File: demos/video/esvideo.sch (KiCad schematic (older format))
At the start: 29 parts, among them U8 BT253, U9 BT473

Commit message: Pcbnew: Minor fix in hotkeys. Demos: add an example to use  a local fp-lib-table and local libs, and update schematics and boards.
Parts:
- C32, C33, C34, C35, C36, C37, C52, R15, R22, R23, R24, R36, R37, R38, R42, R43, R44, R45, R46, R47, R8: footprint (none) -> lib_smd:SM1206
- C39, C40, C41, C42, C51: footprint (none) -> lib_smd:SM1210L
- L5: footprint (none) -> lib_smd:SM1812
- U8: footprint (none) -> footprints:PLCC84
- U9: footprint (none) -> footprints:PLCC68

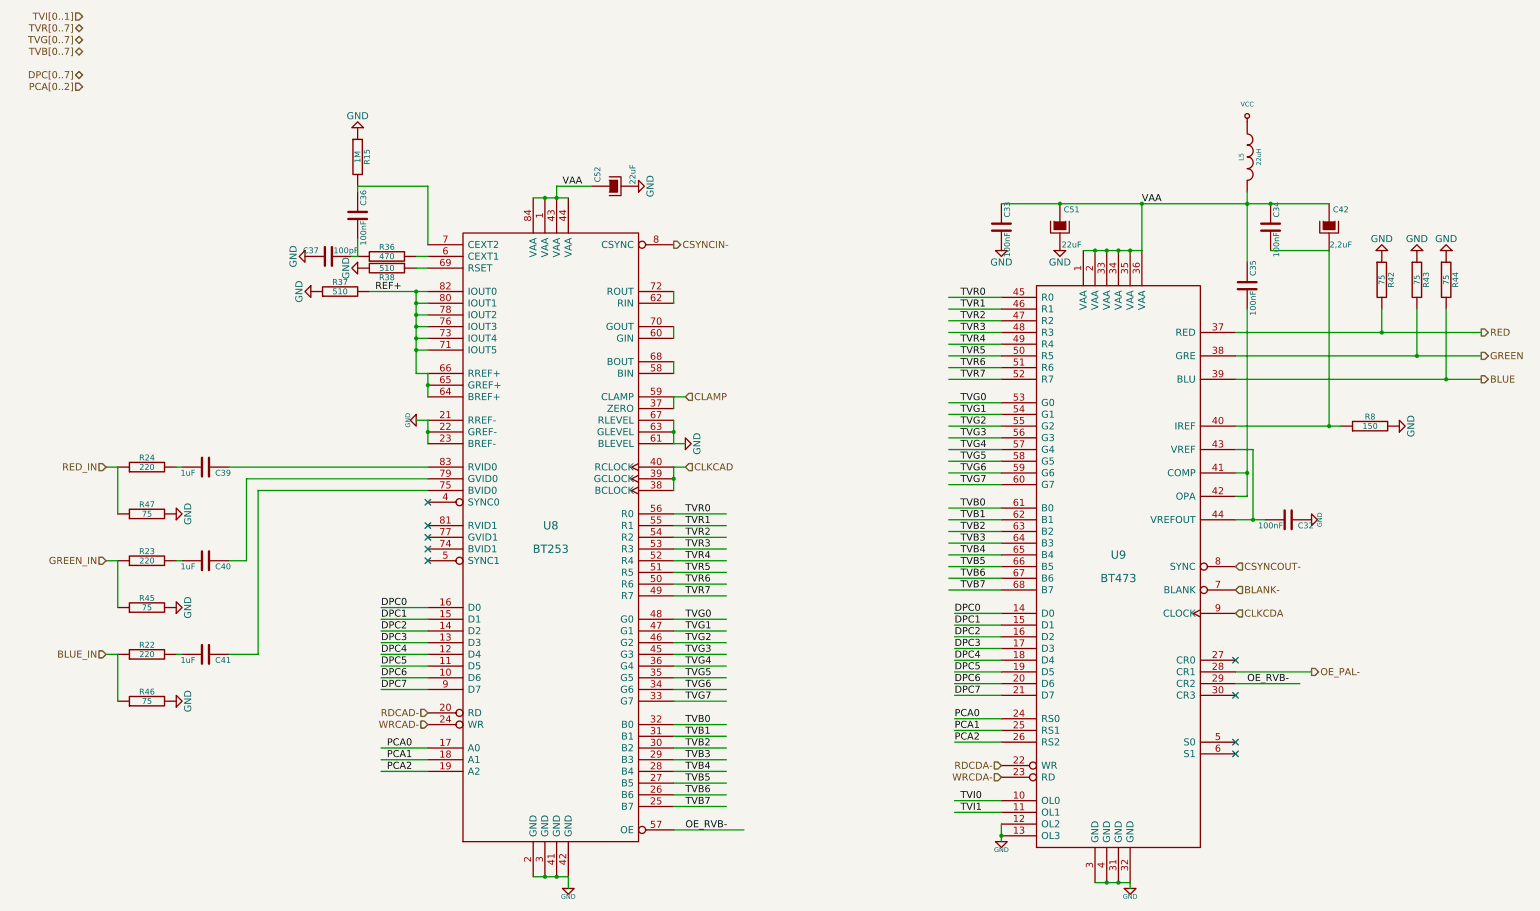
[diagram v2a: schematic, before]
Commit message: demos/ schematic tidying
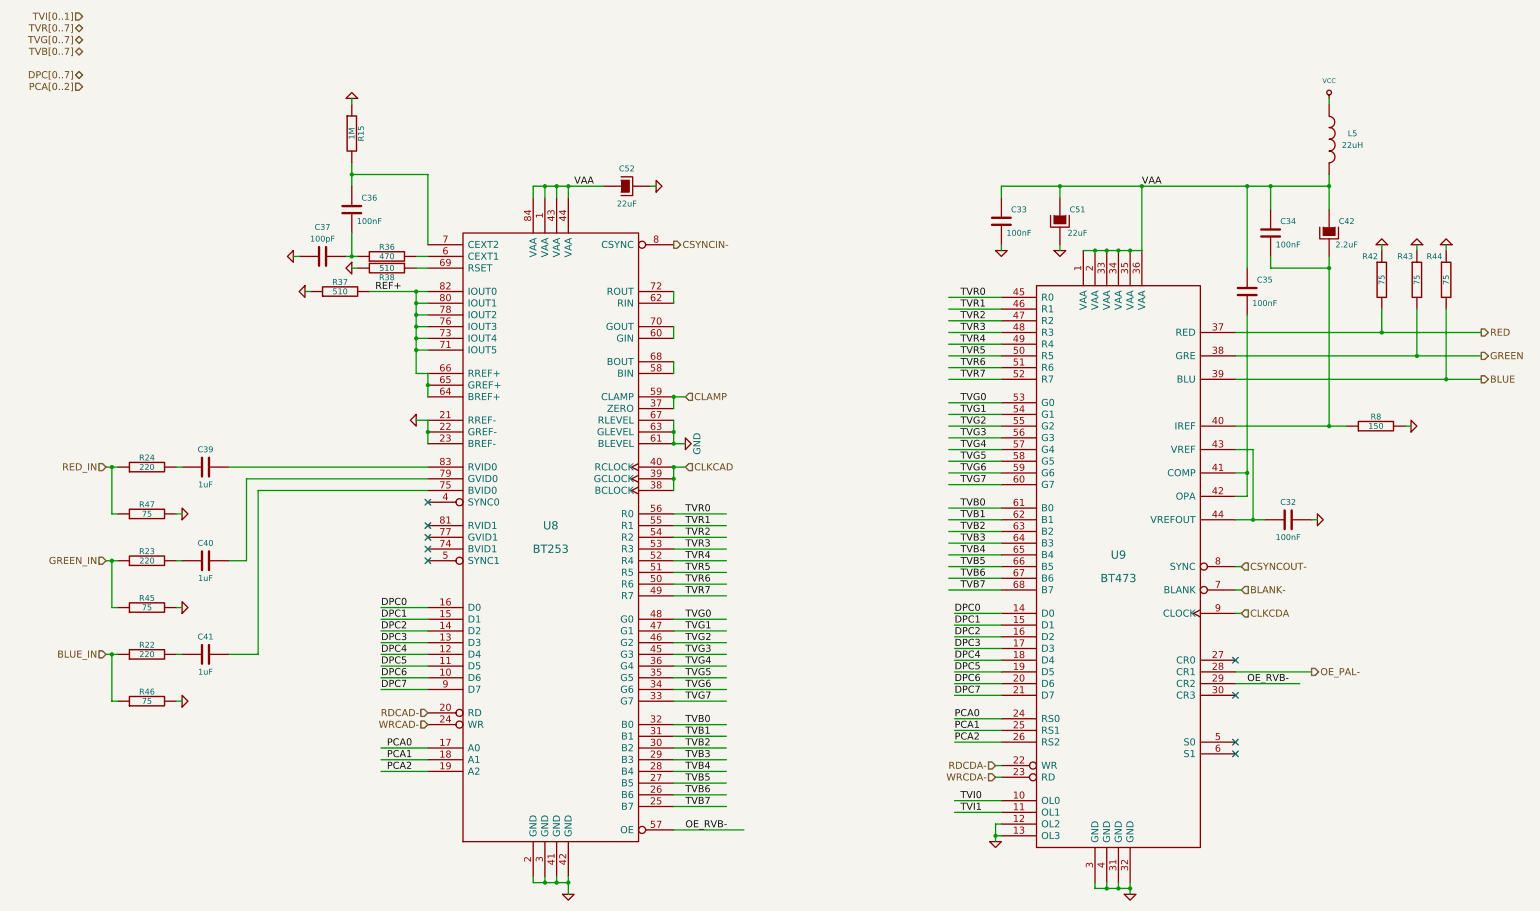
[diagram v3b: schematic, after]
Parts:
- C42: value 2,2uF -> 2.2uF
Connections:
- wire segments 145 -> 184
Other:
- moved on the sheet: C33, C34, C35, C36, C37, C42, C51, C52, L5, R15, R8
